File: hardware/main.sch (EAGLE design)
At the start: 89 parts, among them U1 TMS320F28069_PN_80, U10 TXB0101_DBV_6, U2 TXB0101_DBV_6, U3 SN74ABT541B_DW_20, U4 SN74LVC1G04_DBV_5, U5 SN74LVC4245A_DW_24, U7 Value, U8 Value, U9 SN74LVC4245A_DW_24

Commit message: Finished routing board. Finished cleaning up silkscreen (top).
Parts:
- removed U$6: SST25VF080BS2AF, ControllerCard:SST25VF080BS2AF
- added D17, D18: (no value), SparkFun-LED:LED3MM
- added R36, R37: 240, SparkFun-Resistors:240OHM1/10W1%(0603)
- added U6: SN74ABT541B_DW_20, ControllerCard:SN74ABT541B_DW_20
- U2: value TXB0101_DBV_6 -> SN74LVC4245A_DW_24; device ControllerCard:TXB0101_DBV_6 -> ControllerCard:SN74LVC4245A_DW_24
- U3: value SN74ABT541B_DW_20 -> Value; device ControllerCard:SN74ABT541B_DW_20 -> ControllerCard:SN64BCT25244DW
- U4: value SN74LVC1G04_DBV_5 -> SN74LVC4245A_DW_24; device ControllerCard:SN74LVC1G04_DBV_5 -> ControllerCard:SN74LVC4245A_DW_24
- U5: value SN74LVC4245A_DW_24 -> Value; device ControllerCard:SN74LVC4245A_DW_24 -> ControllerCard:SN64BCT25244DW
- U7: value Value -> SN74LVC1G04_DBV_5; device ControllerCard:SN64BCT25244DW -> ControllerCard:SN74LVC1G04_DBV_5
- U8: value Value -> SST25VF080BS2AF; device ControllerCard:SN64BCT25244DW -> ControllerCard:SST25VF080BS2AF
- U9: value SN74LVC4245A_DW_24 -> TXB0101_DBV_6; device ControllerCard:SN74LVC4245A_DW_24 -> ControllerCard:TXB0101_DBV_6
- renumbered JP2 to USB, U$1 to JTAG, U$10 to SW1, U$11 to SW2, U$2 to !TRST!, U$3 to CRYSTAL, U$5 to LM3940
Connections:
- new net N$41: D17.A, R36.1
- new net N$42: D18.A, R37.1
- net !BUFEN!: now also U2.*OE, U3.1OE_N, U3.2OE_N, U4.*OE; no longer U5.*OE, U8.1OE_N, U8.2OE_N, U9.*OE
- net !FLASHEN!: now also U8.!CE!; no longer U$6.!CE!
- net !FLASHHOLD!: now also U8.!HOLD!; no longer U$6.!HOLD!
- net !FLASHWP!: now also U8.!WP!; no longer U$6.!WP!
- net !INSEL!: now also U6.*OE1, U6.*OE2, U7.Y; no longer U3.*OE1, U3.*OE2, U4.Y
- net 3.3V: now also U1.VDD_6, U2.VCCB, U2.VCCB_2, U4.VCCB, U4.VCCB_2, U8.VCC, U9.VCCA; no longer U$6.VCC, U2.VCCA, U5.VCCB, U5.VCCB_2, U9.VCCB, U9.VCCB_2
- net 5V: now also R36.2, U2.VCCA, U3.VCC_2, U4.DIR, U4.VCCA, U5.VCC, U5.VCC_2, U6.VCC, U9.VCCB; no longer U2.VCCB, U4.VCC, U5.DIR, U5.VCCA, U7.VCC_2, U8.VCC, U8.VCC_2, U9.VCCA
- net ENEXT: now also U9.OE; no longer U2.OE
- net GND: now also D17.C, D18.C, U2.DIR, U2.GND_2, U2.GND_3, U3.GND_2, U3.GND_3, U3.GND_4, U4.GND_2, U4.GND_3, U5.GND_4, U6.GND; no longer U$6.GND, U7.GND_2, U7.GND_3, U7.GND_4, U8.GND_2, U8.GND_3, U8.GND_4, U9.DIR, U9.GND_2, U9.GND_3
- net INSEL: now also U5.1OE_N, U5.2OE_N, U7.A; no longer U4.A, U7.1OE_N, U7.2OE_N
- net LEDIN1: now also U4.A1, U5.1Y1, U6.Y1; no longer U3.Y1, U5.A1, U7.1Y1
- net LEDIN2: now also U4.A2, U5.1Y2, U6.Y2; no longer U3.Y2, U5.A2, U7.1Y2
- net LEDIN3: now also U4.A3, U5.1Y3, U6.Y3; no longer U3.Y3, U5.A3, U7.1Y3
- net LEDIN4: now also U4.A4, U5.1Y4, U6.Y4; no longer U3.Y4, U5.A4, U7.1Y4
- net LEDIN5: now also U4.A5, U5.2Y1, U6.Y5; no longer U3.Y5, U5.A5, U7.2Y1
- net LEDIN6: now also U4.A6, U5.2Y2, U6.Y6; no longer U3.Y6, U5.A6, U7.2Y2
- net LEDIN7: now also U4.A7, U5.2Y3, U6.Y7; no longer U3.Y7, U5.A7, U7.2Y3
- net LEDIN8: now also U4.A8, U5.2Y4, U6.Y8; no longer U3.Y8, U5.A8, U7.2Y4
- net LEDOUT1: now also U2.A1, U3.1A1; no longer U8.1A1, U9.A1
- net LEDOUT2: now also U2.A2, U3.1A2; no longer U8.1A2, U9.A2
- net LEDOUT3: now also U2.A3, U3.1A3; no longer U8.1A3, U9.A3
- net LEDOUT4: now also U2.A4, U3.1A4; no longer U8.1A4, U9.A4
- net LEDOUT5: now also U2.A5, U3.2A1; no longer U8.2A1, U9.A5
- net LEDOUT6: now also U2.A6, U3.2A2; no longer U8.2A2, U9.A6
- net LEDOUT7: now also U2.A7, U3.2A3; no longer U8.2A3, U9.A7
- net LEDOUT8: now also U2.A8, U3.2A4; no longer U8.2A4, U9.A8
- net N$13: now also U3.1Y1; no longer U8.1Y1
- net N$14: now also U3.1Y2; no longer U8.1Y2
- net N$15: now also U3.1Y3; no longer U8.1Y3
- net N$16: now also U3.1Y4; no longer U8.1Y4
- net N$17: now also U3.2Y4; no longer U8.2Y4
- net N$18: now also U3.2Y3; no longer U8.2Y3
- net N$19: now also U3.2Y2; no longer U8.2Y2
- net N$2: now also R37.2, U9.B; no longer U2.B
- net N$20: now also U3.2Y1; no longer U8.2Y1
- net N$21: now also U5.1A1; no longer U7.1A1
- net N$22: now also U5.1A2; no longer U7.1A2
- net N$23: now also U5.1A3; no longer U7.1A3
- net N$24: now also U5.1A4; no longer U7.1A4
- net N$25: now also U5.2A4; no longer U7.2A4
- net N$26: now also U5.2A3; no longer U7.2A3
- net N$27: now also U5.2A2; no longer U7.2A2
- net N$28: now also U5.2A1; no longer U7.2A1
- net SPICLK: now also U8.SCK; no longer U$6.SCK
- net SPISIMO: now also U8.SI; no longer U$6.SI
- net SPISOMI: now also U8.SO; no longer U$6.SO
- net SW1: now also U6.A1; no longer U3.A1
- net SW2: now also U6.A2; no longer U3.A2
- net SW3: now also U6.A3; no longer U3.A3
- net SW4: now also U6.A4; no longer U3.A4
- net SW5: now also U6.A5; no longer U3.A5
- net SW6: now also U6.A6; no longer U3.A6
- net SW7: now also U6.A7; no longer U3.A7
- net SW8: now also U6.A8; no longer U3.A8
- net UCIN1: now also U4.B1; no longer U5.B1
- net UCIN2: now also U4.B3; no longer U5.B3
- net UCIN3: now also U4.B3_2; no longer U5.B3_2
- net UCIN4: now also U4.B4; no longer U5.B4
- net UCIN5: now also U4.B5; no longer U5.B5
- net UCIN6: now also U4.B6; no longer U5.B6
- net UCIN7: now also U4.B7; no longer U5.B7
- net UCIN8: now also U4.B8; no longer U5.B8
- net UCOUT1: now also U2.B1; no longer U9.B1
- net UCOUT2: now also U2.B3; no longer U9.B3
- net UCOUT3: now also U2.B3_2; no longer U9.B3_2
- net UCOUT4: now also U2.B4; no longer U9.B4
- net UCOUT5: now also U2.B5; no longer U9.B5
- net UCOUT6: now also U2.B6; no longer U9.B6
- net UCOUT7: now also U2.B7; no longer U9.B7
- net UCOUT8: now also U2.B8; no longer U9.B8
- net USBMON: now also U9.A; no longer U2.A
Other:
- moved on the sheet: JP1, U5

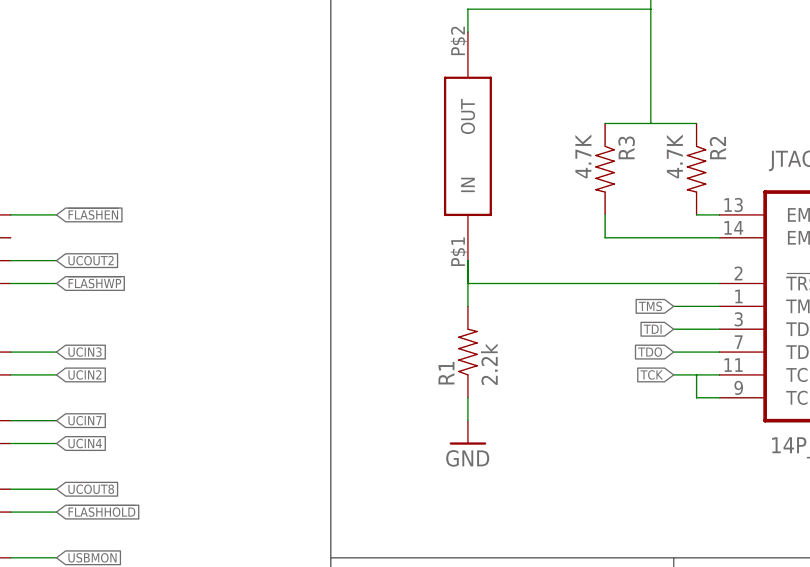
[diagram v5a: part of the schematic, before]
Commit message: Fixed minor error with JTAG. TRST pin not connected
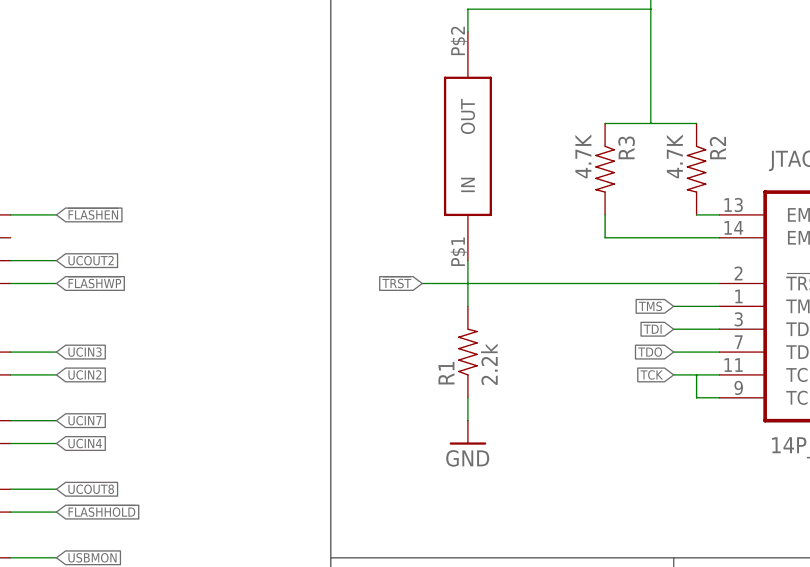
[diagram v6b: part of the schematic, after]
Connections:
- removed net N$1: !TRST!.IN, JTAG.!TRST!, R1.2
- net !TRST!: now also !TRST!.IN, JTAG.!TRST!, R1.2
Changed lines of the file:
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@@
 <grid distance="0.1" unitdist="inch" unit="inch" style="lines" multiple="1" display="no" altdistance="0.01" altunitdist="inch" altunit="inch"/>
 <layers>
-<layer number="1" name="Top" color="4" fill="1" visible="yes" active="no"/>
-<layer number="2" name="Route2" color="1" fill="3" visible="yes" active="no"/>
-<layer number="3" name="Route3" color="4" fill="3" visible="yes" active="no"/>
-<layer number="4" name="Route4" color="1" fill="4" visible="yes" active="no"/>
-<layer number="5" name="Route5" color="4" fill="4" visible="yes" active="no"/>
-<layer number="6" name="Route6" color="1" fill="8" visible="yes" active="no"/>
-<layer number="7" name="Route7" color="4" fill="8" visible="yes" active="no"/>
-<layer number="8" name="Route8" color="1" fill="2" visible="yes" active="no"/>
-<layer number="9" name="Route9" color="4" fill="2" visible="yes" active="no"/>
-<layer number="10" name="Route10" color="1" fill="7" visible="yes" active="no"/>
-<layer number="11" name="Route11" color="4" fill="7" visible="yes" active="no"/>
-<layer number="12" name="Route12" color="1" fill="5" visible="yes" active="no"/>
-<layer number="13" name="Route13" color="4" fill="5" visible="yes" active="no"/>
-<layer number="14" name="Route14" color="1" fill="6" visible="yes" active="no"/>
-<layer number="15" name="Route15" color="4" fill="6" visible="yes" active="no"/>
-<layer number="16" name="Bottom" color="1" fill="1" visible="yes" active="no"/>
-<layer number="17" name="Pads" color="2" fill="1" visible="yes" active="no"/>
-<layer number="18" name="Vias" color="2" fill="1" visible="yes" active="no"/>
-<layer number="19" name="Unrouted" color="6" fill="1" visible="yes" active="no"/>
-<layer number="20" name="Dimension" color="15" fill="1" visible="yes" active="no"/>
-<layer number="21" name="tPlace" color="7" fill="1" visible="yes" active="no"/>
-<layer number="22" name="bPlace" color="7" fill="1" visible="yes" active="no"/>
-<layer number="23" name="tOrigins" color="15" fill="1" visible="yes" active="no"/>
-<layer number="24" name="bOrigins" color="15" fill="1" visible="yes" active="no"/>
-<layer number="25" name="tNames" color="7" fill="1" visible="yes" active="no"/>
-<layer number="26" name="bNames" color="7" fill="1" visible="yes" active="no"/>
-<layer number="27" name="tValues" color="7" fill="1" visible="yes" active="no"/>
-<layer number="28" name="bValues" color="7" fill="1" visible="yes" active="no"/>
+<layer number="1" name="Top" color="4" fill="1" visible="no" active="no"/>
+<layer number="2" name="Route2" color="1" fill="3" visible="no" active="no"/>
+<layer number="3" name="Route3" color="4" fill="3" visible="no" active="no"/>
+<layer number="4" name="Route4" color="1" fill="4" visible="no" active="no"/>
+<layer number="5" name="Route5" color="4" fill="4" visible="no" active="no"/>
+<layer number="6" name="Route6" color="1" fill="8" visible="no" active="no"/>
+<layer number="7" name="Route7" color="4" fill="8" visible="no" active="no"/>
+<layer number="8" name="Route8" color="1" fill="2" visible="no" active="no"/>
+<layer number="9" name="Route9" color="4" fill="2" visible="no" active="no"/>
+<layer number="10" name="Route10" color="1" fill="7" visible="no" active="no"/>
+<layer number="11" name="Route11" color="4" fill="7" visible="no" active="no"/>
+<layer number="12" name="Route12" color="1" fill="5" visible="no" active="no"/>
+<layer number="13" name="Route13" color="4" fill="5" visible="no" active="no"/>
+<layer number="14" name="Route14" color="1" fill="6" visible="no" active="no"/>
+<layer number="15" name="Route15" color="4" fill="6" visible="no" active="no"/>
+<layer number="16" name="Bottom" color="1" fill="1" visible="no" active="no"/>
+<layer number="17" name="Pads" color="2" fill="1" visible="no" active="no"/>
+<layer number="18" name="Vias" color="2" fill="1" visible="no" active="no"/>
+<layer number="19" name="Unrouted" color="6" fill="1" visible="no" active="no"/>
+<layer number="20" name="Dimension" color="15" fill="1" visible="no" active="no"/>
+<layer number="21" name="tPlace" color="7" fill="1" visible="no" active="no"/>
+<layer number="22" name="bPlace" color="7" fill="1" visible="no" active="no"/>
+<layer number="23" name="tOrigins" color="15" fill="1" visible="no" active="no"/>
+<layer number="24" name="bOrigins" color="15" fill="1" visible="no" active="no"/>
+<layer number="25" name="tNames" color="7" fill="1" visible="no" active="no"/>
+<layer number="26" name="bNames" color="7" fill="1" visible="no" active="no"/>
+<layer number="27" name="tValues" color="7" fill="1" visible="no" active="no"/>
+<layer number="28" name="bValues" color="7" fill="1" visible="no" active="no"/>
 <layer number="29" name="tStop" color="7" fill="3" visible="no" active="no"/>
 <layer number="30" name="bStop" color="7" fill="6" visible="no" active="no"/>
@@
 <layer number="35" name="tGlue" color="7" fill="4" visible="no" active="no"/>
 <layer number="36" name="bGlue" color="7" fill="5" visible="no" active="no"/>
-<layer number="37" name="tTest" color="7" fill="1" visible="yes" active="no"/>
-<layer number="38" name="bTest" color="7" fill="1" visible="yes" active="no"/>
+<layer number="37" name="tTest" color="7" fill="1" visible="no" active="no"/>
+<layer number="38" name="bTest" color="7" fill="1" visible="no" active="no"/>
 <layer number="39" name="tKeepout" color="4" fill="11" visible="no" active="no"/>
 <layer number="40" name="bKeepout" color="1" fill="11" visible="no" active="no"/>
@@
 <layer number="44" name="Drills" color="7" fill="1" visible="no" active="no"/>
 <layer number="45" name="Holes" color="7" fill="1" visible="no" active="no"/>
-<layer number="46" name="Milling" color="3" fill="1" visible="yes" active="no"/>
-<layer number="47" name="Measures" color="7" fill="1" visible="yes" active="no"/>
-<layer number="48" name="Document" color="7" fill="1" visible="yes" active="no"/>
-<layer number="49" name="Reference" color="7" fill="1" visible="yes" active="no"/>
-<layer number="50" name="dxf" color="7" fill="1" visible="yes" active="no"/>
-<layer number="51" name="tDocu" color="7" fill="1" visible="yes" active="no"/>
-<layer number="52" name="bDocu" color="7" fill="1" visible="yes" active="no"/>
-<layer number="53" name="tGND_GNDA" color="7" fill="9" visible="yes" active="no"/>
-<layer number="54" name="bGND_GNDA" color="1" fill="9" visible="yes" active="no"/>
-<layer number="56" name="wert" color="7" fill="1" visible="yes" active="no"/>
-<layer number="57" name="tCAD" color="7" fill="1" visible="yes" active="no"/>
+<layer number="46" name="Milling" color="3" fill="1" visible="no" active="no"/>
+<layer number="47" name="Measures" color="7" fill="1" visible="no" active="no"/>
+<layer number="48" name="Document" color="7" fill="1" visible="no" active="no"/>
+<layer number="49" name="Reference" color="7" fill="1" visible="no" active="no"/>
+<layer number="50" name="dxf" color="7" fill="1" visible="no" active="no"/>
+<layer number="51" name="tDocu" color="7" fill="1" visible="no" active="no"/>
+<layer number="52" name="bDocu" color="7" fill="1" visible="no" active="no"/>
+<layer number="53" name="tGND_GNDA" color="7" fill="9" visible="no" active="no"/>
+<layer number="54" name="bGND_GNDA" color="1" fill="9" visible="no" active="no"/>
+<layer number="56" name="wert" color="7" fill="1" visible="no" active="no"/>
+<layer number="57" name="tCAD" color="7" fill="1" visible="no" active="no"/>
 <layer number="90" name="Modules" color="5" fill="1" visible="yes" active="yes"/>
 <layer number="91" name="Nets" color="2" fill="1" visible="yes" active="yes"/>
@@
 <label x="40.64" y="76.2" size="1.016" layer="95" rot="R180" xref="yes"/>
 </segment>
+<segment>
+<pinref part="JTAG" gate="G$1" pin="!TRST!"/>
+<pinref part="!TRST!" gate="G$1" pin="IN"/>
+<wire x1="307.34" y1="139.7" x2="279.4" y2="139.7" width="0.1524" layer="91"/>
+<pinref part="R1" gate="G$1" pin="2"/>
+<wire x1="279.4" y1="142.24" x2="279.4" y2="139.7" width="0.1524" layer="91"/>
+<wire x1="279.4" y1="139.7" x2="279.4" y2="137.16" width="0.1524" layer="91"/>
+<wire x1="279.4" y1="139.7" x2="274.32" y2="139.7" width="0.1524" layer="91"/>
+<label x="274.32" y="139.7" size="1.016" layer="95" rot="R180" xref="yes"/>
+</segment>
 </net>
 <net name="X1" class="0">
@@
 </segment>
 </net>
-<net name="N$1" class="0">
-<segment>
-<pinref part="JTAG" gate="G$1" pin="!TRST!"/>
-<pinref part="!TRST!" gate="G$1" pin="IN"/>
-<wire x1="307.34" y1="139.7" x2="279.4" y2="139.7" width="0.1524" layer="91"/>
-<wire x1="279.4" y1="139.7" x2="279.4" y2="142.24" width="0.1524" layer="91"/>
-<pinref part="R1" gate="G$1" pin="2"/>
-<wire x1="279.4" y1="142.24" x2="279.4" y2="137.16" width="0.1524" layer="91"/>
-</segment>
-</net>

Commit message: Routed un-noticed airwires. Tried to add SPI breakout. Unsuccessful
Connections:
- new net CE1: U1.GPIO2/EPWM2A
- new net CE2: U1.GPIO0/EPWM1A
- new net CE3: U1.GPIO15/ECAP2/SCIRXDB/*SPISTEB
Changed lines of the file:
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@@
+</segment>
+</net>
+<net name="CE3" class="0">
+<segment>
+<pinref part="U1" gate="A" pin="GPIO15/ECAP2/SCIRXDB/*SPISTEB"/>
+<wire x1="228.6" y1="83.82" x2="233.68" y2="83.82" width="0.1524" layer="91"/>
+<label x="233.68" y="83.82" size="1.016" layer="95" xref="yes"/>
+</segment>
+</net>
+<net name="CE2" class="0">
+<segment>
+<pinref part="U1" gate="A" pin="GPIO0/EPWM1A"/>
+<wire x1="228.6" y1="40.64" x2="233.68" y2="40.64" width="0.1524" layer="91"/>
+<label x="233.68" y="40.64" size="1.016" layer="95" xref="yes"/>
+</segment>
+</net>
+<net name="CE1" class="0">
+<segment>
+<pinref part="U1" gate="A" pin="GPIO2/EPWM2A"/>
+<wire x1="228.6" y1="38.1" x2="233.68" y2="38.1" width="0.1524" layer="91"/>
+<label x="233.68" y="38.1" size="1.016" layer="95" xref="yes"/>
 </segment>
 </net>

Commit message: Added SPI breakout. Routed and updated silkscreen for SPI breakout
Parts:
- added JP2: FEMALE 2x3, SparkFun-Connectors:M03X2FEMALE
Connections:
- removed net CE2: U1.GPIO0/EPWM1A
- removed net CE3: U1.GPIO15/ECAP2/SCIRXDB/*SPISTEB
- net 3.3V: now also JP2.5
- net CE1: now also JP2.4, U1.GPIO10/EPWM6A/*ADCSOCBO; no longer U1.GPIO2/EPWM2A
- net GND: now also JP2.6
- net SPICLK: now also JP2.1
- net SPISIMO: now also JP2.2
- net SPISOMI: now also JP2.3
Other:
- note added: "SPI Breakout"
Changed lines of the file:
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@@
 <part name="R37" library="SparkFun-Resistors" deviceset="240OHM1/10W1%(0603)" device="" value="240"/>
 <part name="GND32" library="SparkFun-Aesthetics" deviceset="GND" device=""/>
+<part name="JP2" library="SparkFun-Connectors" deviceset="M03X2" device="FEMALE" value="FEMALE 2x3"/>
+<part name="SUPPLY25" library="SparkFun-Aesthetics" deviceset="3.3V" device=""/>
+<part name="GND33" library="SparkFun-Aesthetics" deviceset="GND" device=""/>
 </parts>
 <sheets>
@@
 <text x="459.74" y="38.1" size="2.54" layer="97">Slide Switches</text>
 <wire x1="457.2" y1="0" x2="574.04" y2="0" width="0.1524" layer="97"/>
-<wire x1="574.04" y1="0" x2="574.04" y2="45.72" width="0.1524" layer="97"/>
+<wire x1="574.04" y1="0" x2="574.04" y2="35.56" width="0.1524" layer="97"/>
+<wire x1="574.04" y1="35.56" x2="574.04" y2="45.72" width="0.1524" layer="97"/>
+<wire x1="574.04" y1="0" x2="624.84" y2="0" width="0.1524" layer="97"/>
+<wire x1="624.84" y1="0" x2="624.84" y2="45.72" width="0.1524" layer="97"/>
+<wire x1="624.84" y1="45.72" x2="599.44" y2="45.72" width="0.1524" layer="97"/>
+<wire x1="574.04" y1="35.56" x2="599.44" y2="35.56" width="0.1524" layer="97"/>
+<wire x1="599.44" y1="35.56" x2="599.44" y2="45.72" width="0.1524" layer="97"/>
+<text x="576.58" y="38.1" size="2.54" layer="97">SPI Breakout</text>
 </plain>
 <instances>
@@
 <instance part="R37" gate="G$1" x="431.8" y="66.04"/>
 <instance part="GND32" gate="1" x="424.18" y="50.8"/>
+<instance part="JP2" gate="G$1" x="596.9" y="22.86"/>
+<instance part="SUPPLY25" gate="G$1" x="576.58" y="27.94"/>
+<instance part="GND33" gate="1" x="607.06" y="15.24"/>
 </instances>
 <busses>
@@
 <wire x1="515.62" y1="22.86" x2="515.62" y2="25.4" width="0.1524" layer="91"/>
 </segment>
+<segment>
+<pinref part="SUPPLY25" gate="G$1" pin="3.3V"/>
+<pinref part="JP2" gate="G$1" pin="5"/>
+<wire x1="576.58" y1="27.94" x2="576.58" y2="20.32" width="0.1524" layer="91"/>
+<wire x1="576.58" y1="20.32" x2="589.28" y2="20.32" width="0.1524" layer="91"/>
+</segment>
 </net>
 <net name="GND" class="0">
@@
 <wire x1="424.18" y1="55.88" x2="424.18" y2="53.34" width="0.1524" layer="91"/>
 </segment>
+<segment>
+<pinref part="JP2" gate="G$1" pin="6"/>
+<pinref part="GND33" gate="1" pin="GND"/>
+<wire x1="604.52" y1="20.32" x2="607.06" y2="20.32" width="0.1524" layer="91"/>
+<wire x1="607.06" y1="20.32" x2="607.06" y2="17.78" width="0.1524" layer="91"/>
+</segment>
 </net>
 <net name="TDI" class="0">
@@
 <label x="233.68" y="71.12" size="1.016" layer="95" xref="yes"/>
 </segment>
+<segment>
+<pinref part="JP2" gate="G$1" pin="1"/>
+<wire x1="589.28" y1="25.4" x2="586.74" y2="25.4" width="0.1524" layer="91"/>
+<label x="586.74" y="25.4" size="1.016" layer="95" rot="R180" xref="yes"/>
+</segment>
 </net>
 <net name="SPISIMO" class="0">
@@
 <label x="233.68" y="73.66" size="1.016" layer="95" xref="yes"/>
 </segment>
+<segment>
+<pinref part="JP2" gate="G$1" pin="2"/>
+<wire x1="604.52" y1="25.4" x2="607.06" y2="25.4" width="0.1524" layer="91"/>
+<label x="607.06" y="25.4" size="1.016" layer="95" xref="yes"/>
+</segment>
 </net>
 <net name="SPISOMI" class="0">
@@
 <wire x1="228.6" y1="81.28" x2="233.68" y2="81.28" width="0.1524" layer="91"/>
 <label x="233.68" y="81.28" size="1.016" layer="95" xref="yes"/>
+</segment>
+<segment>
+<pinref part="JP2" gate="G$1" pin="3"/>
+<wire x1="589.28" y1="22.86" x2="586.74" y2="22.86" width="0.1524" layer="91"/>
+<label x="586.74" y="22.86" size="1.016" layer="95" rot="R180" xref="yes"/>
 </segment>
 </net>
@@
 </segment>
 </net>
-<net name="CE3" class="0">
-<segment>
-<pinref part="U1" gate="A" pin="GPIO15/ECAP2/SCIRXDB/*SPISTEB"/>
-<wire x1="228.6" y1="83.82" x2="233.68" y2="83.82" width="0.1524" layer="91"/>
-<label x="233.68" y="83.82" size="1.016" layer="95" xref="yes"/>
-</segment>
-</net>
-<net name="CE2" class="0">
-<segment>
-<pinref part="U1" gate="A" pin="GPIO0/EPWM1A"/>
-<wire x1="228.6" y1="40.64" x2="233.68" y2="40.64" width="0.1524" layer="91"/>
-<label x="233.68" y="40.64" size="1.016" layer="95" xref="yes"/>
-</segment>
-</net>
 <net name="CE1" class="0">
 <segment>
-<pinref part="U1" gate="A" pin="GPIO2/EPWM2A"/>
-<wire x1="228.6" y1="38.1" x2="233.68" y2="38.1" width="0.1524" layer="91"/>
-<label x="233.68" y="38.1" size="1.016" layer="95" xref="yes"/>
-</segment>
-</net>
+<pinref part="JP2" gate="G$1" pin="4"/>
+<wire x1="604.52" y1="22.86" x2="607.06" y2="22.86" width="0.1524" layer="91"/>
+<label x="607.06" y="22.86" size="1.016" layer="95" xref="yes"/>
+</segment>
+<segment>
+<pinref part="U1" gate="A" pin="GPIO10/EPWM6A/*ADCSOCBO"/>
+<wire x1="228.6" y1="144.78" x2="233.68" y2="144.78" width="0.1524" layer="91"/>
+<label x="233.68" y="144.78" size="1.016" layer="95" xref="yes"/>
+</segment>
+</net>
